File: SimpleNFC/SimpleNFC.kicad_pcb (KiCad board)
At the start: 2 copper layers, 32.5 x 41 mm, 14 parts, among them J1 ICSP, U1 ATtiny84A-P, Y1 13.5925Mhz

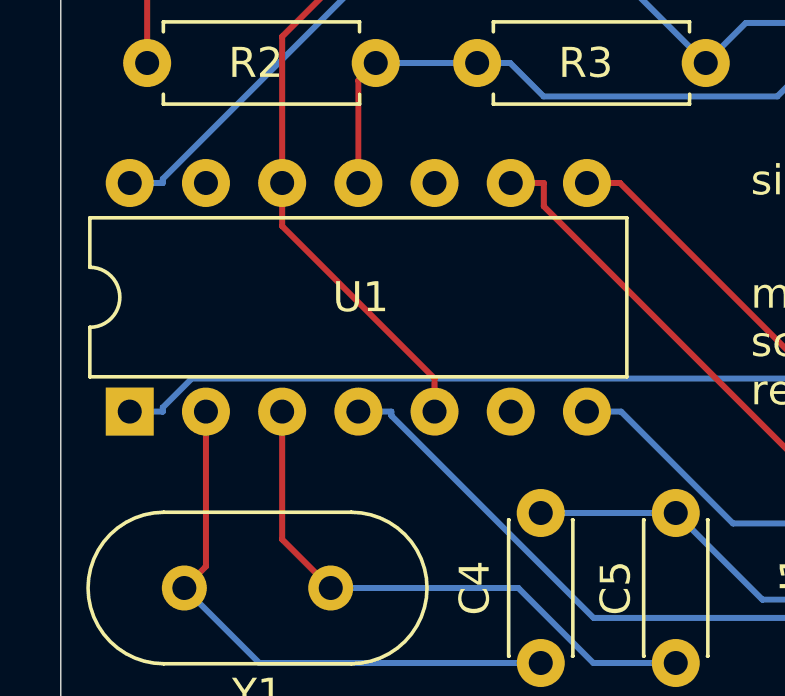
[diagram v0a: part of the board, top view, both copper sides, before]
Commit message: fix design, add firmware, build script
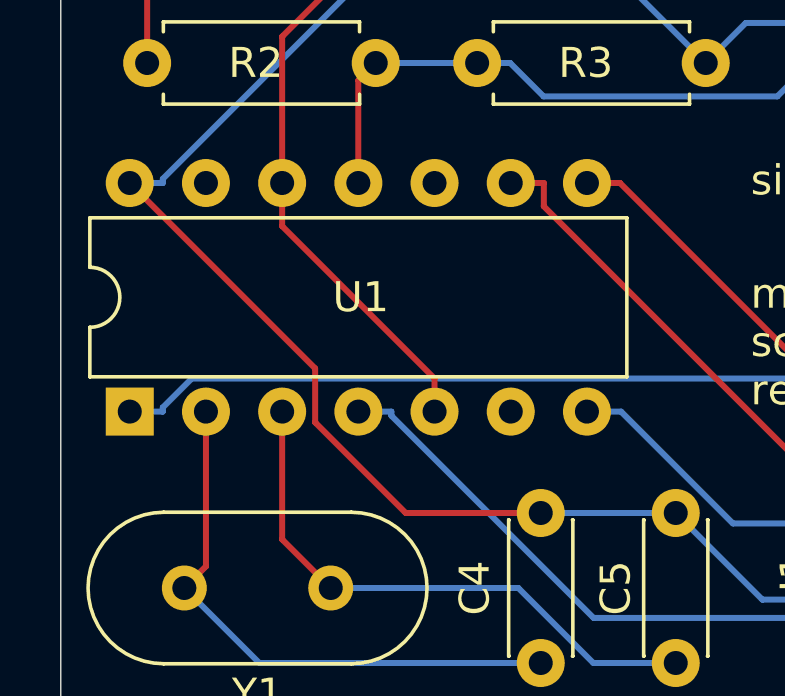
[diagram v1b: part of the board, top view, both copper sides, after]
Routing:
- net GND: track 71.3 -> 90.6 mm
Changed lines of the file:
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@@
+	)
+	(segment
+		(start 128.5 93.5)
+		(end 124 93.5)
+		(width 0.2)
+		(layer "F.Cu")
+		(net 2)
+	)
+	(segment
+		(start 120.98 88.68)
+		(end 114.8 82.5)
+		(width 0.2)
+		(layer "F.Cu")
+		(net 2)
+	)
+	(segment
+		(start 120.98 90.48)
+		(end 120.98 88.68)
+		(width 0.2)
+		(layer "F.Cu")
+		(net 2)
+	)
+	(segment
+		(start 124 93.5)
+		(end 120.98 90.48)
+		(width 0.2)
+		(layer "F.Cu")
+		(net 2)
 	)
 	(segment
